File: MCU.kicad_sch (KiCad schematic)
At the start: 9 parts, among them J101 DC_Con, U101 BluePill

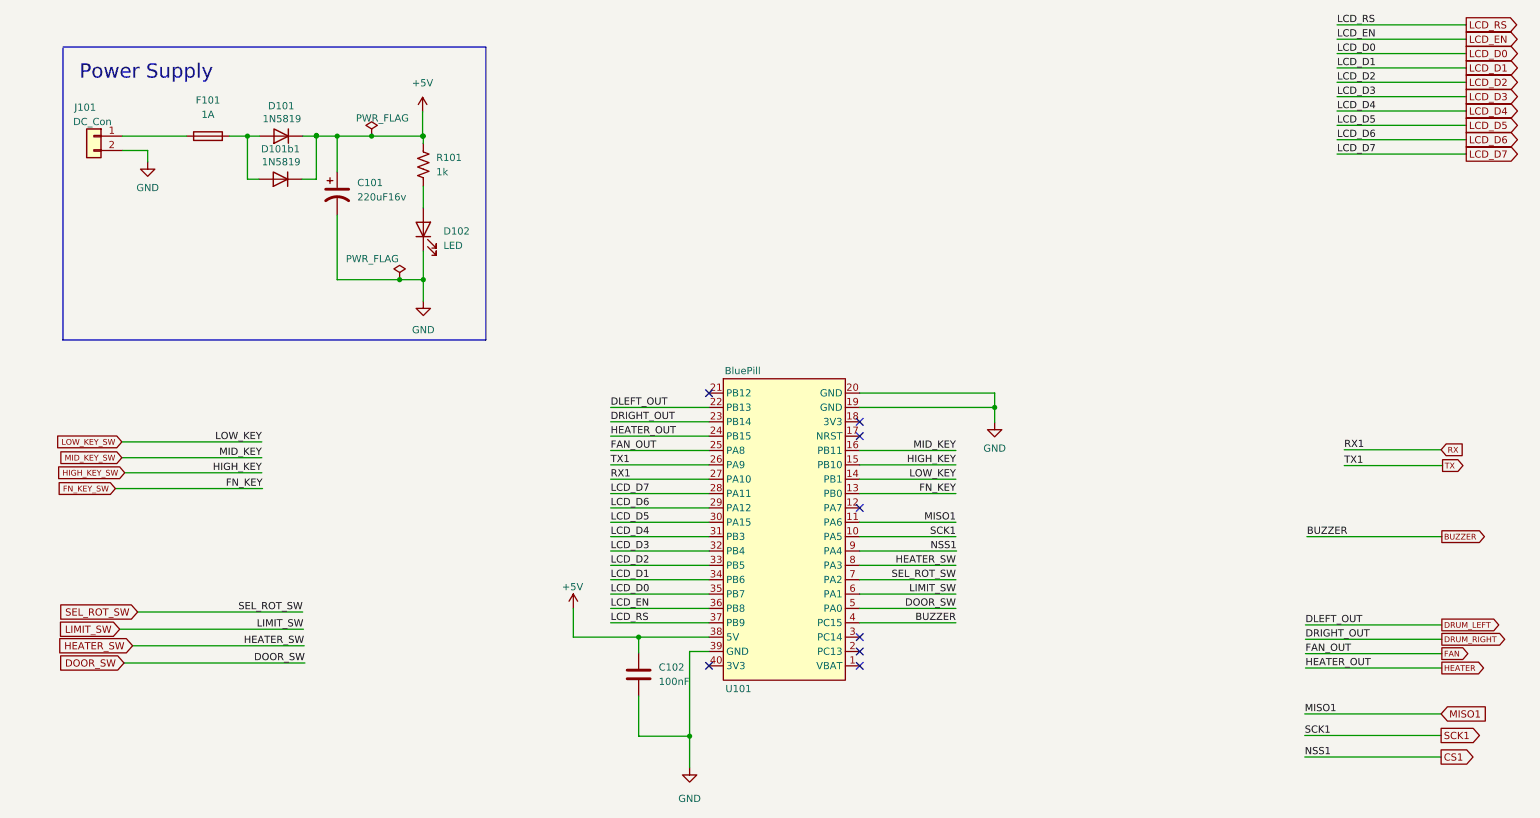
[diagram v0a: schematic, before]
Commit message: Added 24v to 5v SMPS, Reduced it to 2 Story, Used Small Relays
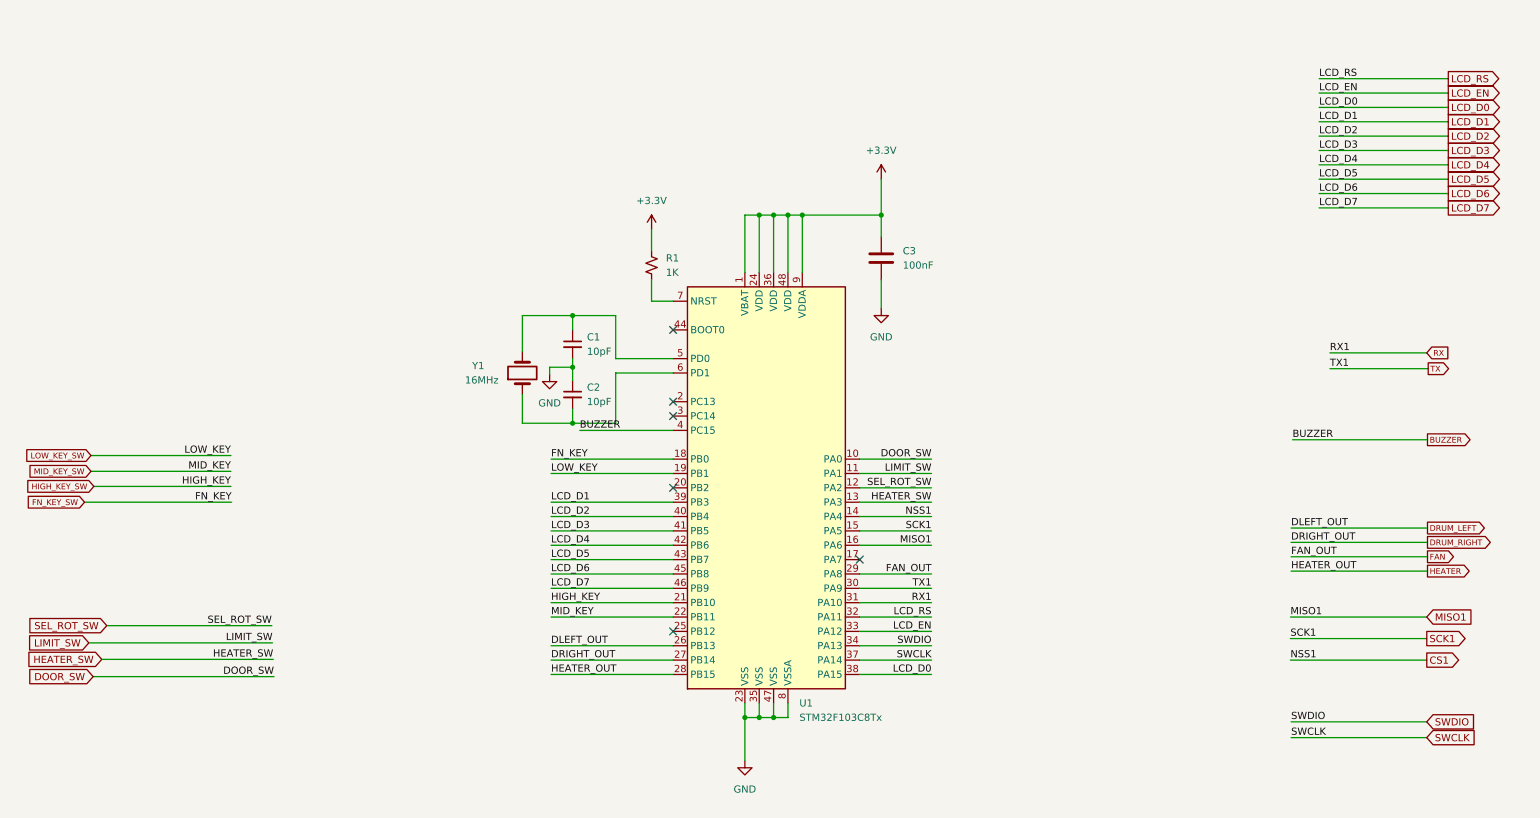
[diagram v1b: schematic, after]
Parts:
- removed C101: 220uF16v, User_Capacitor_THT:CP_Radial_D8.0mm_P5.00mm, symbol Device:C_Polarized_US
- removed C102: 100nF, User_Capacitor_THT:C_Disc_D4.3mm_W1.9mm_P5.00mm, symbol Device:C
- removed D101, D101b1: 1N5819, User_Diode_THT:D_A-405_P7.62mm_Horizontal, symbol Device:D
- removed D102: LED, User_LED_THT:LED_D3.0mm, symbol Device:LED
- removed F101: 1A, User_Fuse:Fuse_Littelfuse_395Series, symbol Device:Fuse
- removed J101: DC_Con, User_Connector_Phoenix_MC_HighVoltage:PhoenixContact_MCV_1,5_2-G-5.08_1x02_P5.08mm_Vertical, symbol Connector_Generic:Conn_01x02
- removed R101: 1k, User_Resostor_THT:R_Axial_DIN0207_L6.3mm_D2.5mm_P10.16mm_Horizontal, symbol Device:R_US
- removed U101: BluePill, STMBoards:BluePill, symbol STM32Board:BluePill
- added C1, C2: 10pF, Capacitor_THT:C_Disc_D3.0mm_W1.6mm_P2.50mm, symbol Device:C_Small
- added C3: 100nF, Capacitor_THT:C_Disc_D4.3mm_W1.9mm_P5.00mm, symbol Device:C
- added R1: 1K, Resistor_THT:R_Axial_DIN0207_L6.3mm_D2.5mm_P10.16mm_Horizontal, symbol Device:R_Small_US
- added U1: STM32F103C8Tx, Package_QFP:LQFP-48_7x7mm_P0.5mm, symbol MCU_ST_STM32F1:STM32F103C8Tx
- added Y1: 16MHz, Crystal:Crystal_HC18-U_Vertical, symbol Device:Crystal
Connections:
- net BUZZER: now also U1.4 (PC15)
- net CS1: now also U1.14 (PA4)
- net DOOR_SW: now also U1.10 (PA0)
- net DRUM_LEFT: now also U1.26 (PB13)
- net DRUM_RIGHT: now also U1.27 (PB14)
- net FAN: now also U1.29 (PA8)
- net FN_KEY_SW: now also U1.18 (PB0)
- net GND: now also C1.2, C2.1, C3.2, U1.23 (VSS), U1.35 (VSS), U1.47 (VSS), U1.8 (VSSA)
- net HEATER: now also U1.28 (PB15)
- net HEATER_SW: now also U1.13 (PA3)
- net HIGH_KEY_SW: now also U1.21 (PB10)
- net LCD_D0: now also U1.38 (PA15)
- net LCD_D1: now also U1.39 (PB3)
- net LCD_D2: now also U1.40 (PB4)
- net LCD_D3: now also U1.41 (PB5)
- net LCD_D4: now also U1.42 (PB6)
- net LCD_D5: now also U1.43 (PB7)
- net LCD_D6: now also U1.45 (PB8)
- net LCD_D7: now also U1.46 (PB9)
- net LCD_EN: now also U1.33 (PA12)
- net LCD_RS: now also U1.32 (PA11)
- net LIMIT_SW: now also U1.11 (PA1)
- net LOW_KEY_SW: now also U1.19 (PB1)
- net MID_KEY_SW: now also U1.22 (PB11)
- net MISO1: now also U1.16 (PA6)
- net RX: now also U1.31 (PA10)
- net SCK1: now also U1.15 (PA5)
- net SEL_ROT_SW: now also U1.12 (PA2)
- net TX: now also U1.30 (PA9)
- new net: C2.2, U1.6 (PD1), Y1.1
- new net: C1.1, U1.5 (PD0), Y1.2
- new net: R1.2, U1.7 (NRST)
- new net +3.3V: C3.1, R1.1, U1.1 (VBAT), U1.24 (VDD), U1.36 (VDD), U1.48 (VDD), U1.9 (VDDA)
- new net SWCLK: U1.37 (PA14)
- new net SWDIO: U1.34 (PA13)
- no-connect marks 8 -> 6
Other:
- note removed: "Power Supply"

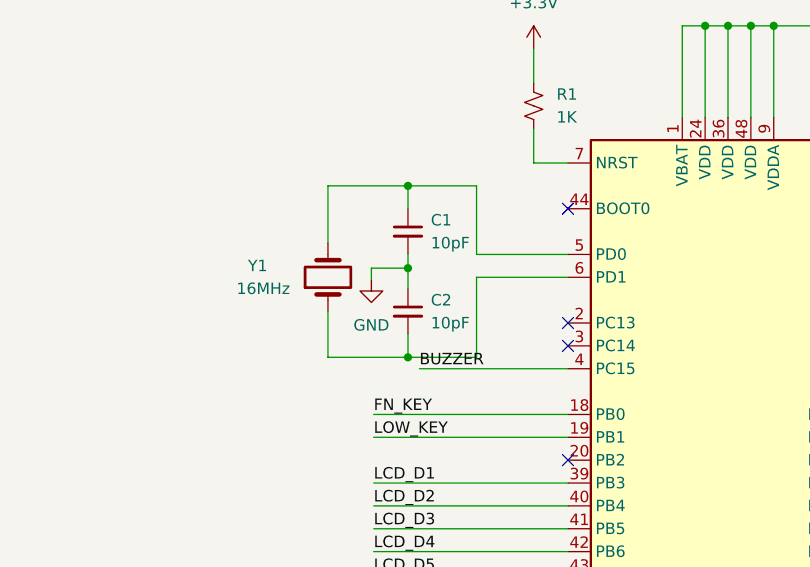
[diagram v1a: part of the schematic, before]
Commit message: Fixed Boot pin not grounded
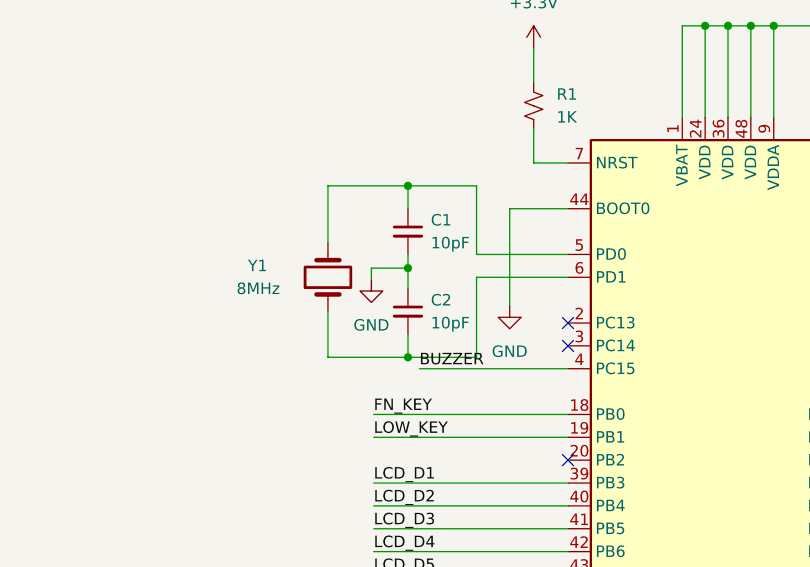
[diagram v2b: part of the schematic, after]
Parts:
- Y1: value 16MHz -> 8MHz
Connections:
- net GND: now also U1.44 (BOOT0)
- no-connect marks 6 -> 5
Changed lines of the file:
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@@
   (no_connect (at 133.35 83.82))
   (no_connect (at 133.35 99.06))
-  (no_connect (at 133.35 71.12))
   (no_connect (at 166.37 111.76))
   (no_connect (at 133.35 124.46))
@@
     (stroke (width 0) (type default) (color 0 0 0 0))
   )
+  (wire (pts (xy 126.873 71.12) (xy 126.873 81.915))
+    (stroke (width 0) (type default) (color 0 0 0 0))
+  )
   (wire (pts (xy 166.37 99.06) (xy 179.07 99.06))
     (stroke (width 0) (type default) (color 0 0 0 0))
@@
   )
   (wire (pts (xy 153.67 50.8) (xy 153.67 60.96))
+    (stroke (width 0) (type default) (color 0 0 0 0))
+  )
+  (wire (pts (xy 133.35 71.12) (xy 126.873 71.12))
     (stroke (width 0) (type default) (color 0 0 0 0))
   )
@@
       (effects (font (size 1.27 1.27)) (justify right))
     )
-    (property "Value" "16MHz" (id 1) (at 96.52 80.01 90)
+    (property "Value" "8MHz" (id 1) (at 96.52 80.01 90)
       (effects (font (size 1.27 1.27)) (justify right))
     )
@@
     (pin "2")
   )
+  (symbol (lib_id "power:GND") (at 126.873 81.915 0) (unit 1)
+    (in_bom yes) (on_board yes) (fields_autoplaced)
+    (property "Reference" "#PWR?" (id 0) (at 126.873 88.265 0)
+      (effects (font (size 1.27 1.27)) hide)
+    )
+    (property "Value" "GND" (id 1) (at 126.873 86.995 0))
+    (property "Footprint" "" (id 2) (at 126.873 81.915 0)
+      (effects (font (size 1.27 1.27)) hide)
+    )
+    (property "Datasheet" "" (id 3) (at 126.873 81.915 0)
+      (effects (font (size 1.27 1.27)) hide)
+    )
+    (pin "1")
+  )
   (symbol (lib_id "Device:R_Small_US") (at 129.54 59.69 0) (unit 1)
